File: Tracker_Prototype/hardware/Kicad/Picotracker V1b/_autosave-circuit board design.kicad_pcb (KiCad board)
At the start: 2 copper layers, 40.4 x 20.1 mm, 57 parts, among them IC7 SPV1040, J1 Conn_01x06, J2 GND, J3 +SOL, J4 BATT_V+, J5 BATT_GND, Q1 Q_PMOS_DGS, Q2 Q_PMOS_DGS, SW1 SW_Push, U2 TPS62740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

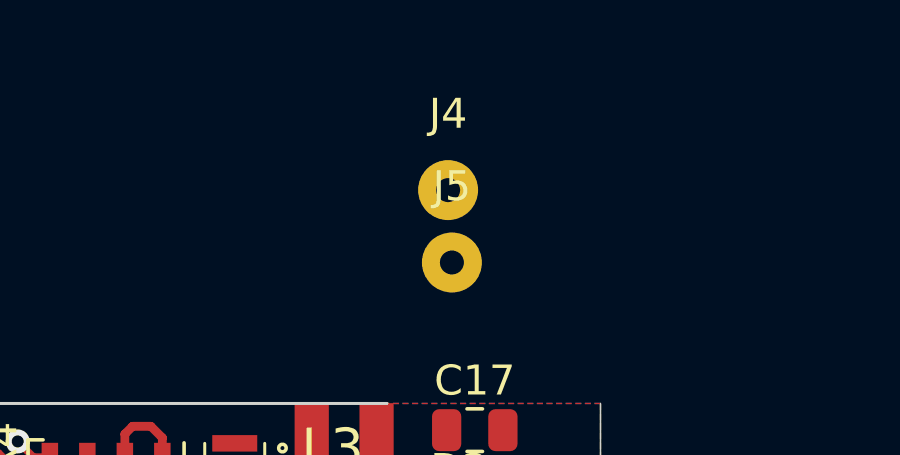
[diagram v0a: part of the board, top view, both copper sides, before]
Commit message: Connected ABZ output pin to GPS back up pin for b variant
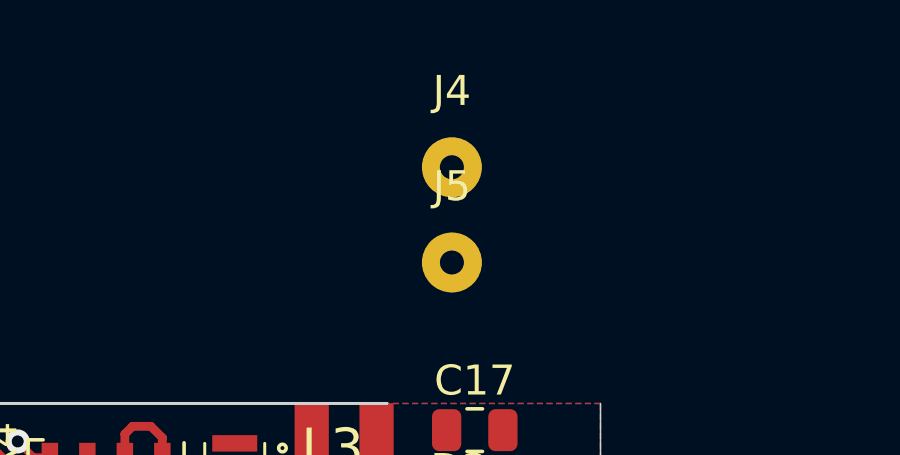
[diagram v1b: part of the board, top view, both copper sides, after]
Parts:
- moved J4 0.77 mm to (299.8, 152.1)
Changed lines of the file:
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@@
   )
   (module Connector_Wire:SolderWirePad_1x01_Drill0.8mm (layer F.Cu)
-    (at 299.72 152.908)
+    (at 299.847 152.146)
     (descr "Wire solder connection")
     (tags connector)
